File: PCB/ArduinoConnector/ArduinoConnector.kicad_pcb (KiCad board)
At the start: 2 copper layers, 0 parts

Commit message: New PCBs
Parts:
- added D1: 1N5819, Diode_SMD:D_SMA, F.Cu at (130.4, 84.0)
- added J1: Arduino, Connector_PinHeader_2.54mm:PinHeader_2x03_P2.54mm_Vertical, F.Cu at (120.2, 92.0)
- added J2: FAN, Connector_Molex:Molex_KK-254_AE-6410-04A_1x04_P2.54mm_Vertical, F.Cu at (128.7, 89.4)
- added Q1: MMBT100, Package_TO_SOT_SMD:SOT-23, F.Cu at (126.7, 85.6)
- added R1: 330, Resistor_SMD:R_0805_2012Metric, F.Cu at (126.7, 82.4)
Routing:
- net +5V: track 0.00 -> 18.7 mm
- net /POWER: track 0.00 -> 14.3 mm
- net /PWM: track 0.00 -> 9.60 mm
- net /SENSE: track 0.00 -> 9.55 mm
- net /FAN_GND: track 0.00 -> 7.80 mm
- net Net-(R1-Pad2): track 0.00 -> 2.28 mm
- net GND: vias 0 -> 6
- added copper zone on B.Cu, net GND
- added copper zone on F.Cu, net GND
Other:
- board outline added: 14.1 x 18.6 mm
- net class Default removed
- net class Power removed
- net class Signal removed

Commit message: Generated gerbers
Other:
- board text added: "ArduinoConnector v1"
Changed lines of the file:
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@@
   )
   (paper "A4")
+  (title_block
+    (title "ArduinoConnector")
+    (date "2022-03-13")
+    (rev "v1")
+  )
   (layers
     (0 "F.Cu" signal)
@@
     (pad_to_mask_clearance 0.0508)
     (pcbplotparams
-      (layerselection 0x0000030_80000001)
+      (layerselection 0x00010f0_ffffffff)
       (disableapertmacros false)
-      (usegerberextensions false)
+      (usegerberextensions true)
       (usegerberattributes true)
       (usegerberadvancedattributes true)
@@
       (outputformat 1)
       (mirror false)
-      (drillshape 1)
+      (drillshape 0)
       (scaleselection 1)
-      (outputdirectory "")
+      (outputdirectory "plots/")
     )
   )
@@
     (fp_line (start -1 0.625) (end -1 -0.625) (layer "F.Fab") (width 0.1))
     (fp_line (start 1 -0.625) (end 1 0.625) (layer "F.Fab") (width 0.1))
-    (pad "1" smd roundrect (at -0.9125 0) (size 1.025 1.4) (layers "F.Cu" "F.Paste" "F.Mask") (roundrect_rratio 0.243902)
+    (pad "1" smd roundrect (at -0.9125 0) (size 1.025 1.4) (layers "F.Cu" "F.Paste" "F.Mask") (roundrect_rratio 0.243902439)
       (net 3 "/POWER") (pintype "passive"))
-    (pad "2" smd roundrect (at 0.9125 0) (size 1.025 1.4) (layers "F.Cu" "F.Paste" "F.Mask") (roundrect_rratio 0.243902)
+    (pad "2" smd roundrect (at 0.9125 0) (size 1.025 1.4) (layers "F.Cu" "F.Paste" "F.Mask") (roundrect_rratio 0.243902439)
       (net 8 "Net-(R1-Pad2)") (pintype "passive"))
     (model "${KICAD6_3DMODEL_DIR}/Resistor_SMD.3dshapes/R_0805_2012Metric.wrl"
@@
     (fp_line (start -0.562893 0) (end -1.27 0.5) (layer "F.Fab") (width 0.1))
     (fp_line (start -1.27 -2.92) (end -1.27 2.88) (layer "F.Fab") (width 0.1))
-    (pad "1" thru_hole roundrect (at 0 0 270) (size 1.74 2.19) (drill 1.19) (layers *.Cu *.Mask) (roundrect_rratio 0.143678)
+    (pad "1" thru_hole roundrect (at 0 0 270) (size 1.74 2.19) (drill 1.19) (layers *.Cu *.Mask) (roundrect_rratio 0.1436781609)
       (net 2 "/FAN_GND") (pinfunction "Pin_1") (pintype "passive"))
     (pad "2" thru_hole oval (at 2.54 0 270) (size 1.74 2.19) (drill 1.19) (layers *.Cu *.Mask)
@@
   (gr_line (start 124.7 90) (end 124.7 80.4) (layer "Edge.Cuts") (width 0.15))
   (gr_line (start 124.7 80.4) (end 132.4 80.4) (layer "Edge.Cuts") (width 0.15))
-  (dimension (type aligned) (layer "F.Cu")
+  (gr_text "ArduinoConnector v1" (at 130.8 89.9 90) (layer "B.SilkS")
+    (effects (font (size 1 1) (thickness 0.15)) (justify mirror))
+  )
+  (dimension (type aligned) (layer "Dwgs.User")
     (pts (xy 132.4 99) (xy 132.4 80.4))
-    (height 5)
-    (gr_text "0.7323 in" (at 135.6 89.7 90) (layer "F.Cu")
+    (height 5.2)
+    (gr_text "18.6000 mm" (at 135.8 89.7 90) (layer "Dwgs.User")
       (effects (font (size 1.5 1.5) (thickness 0.3)))
     )
@@
     (style (thickness 0.2) (arrow_length 1.27) (text_position_mode 0) (extension_height 0.58642) (extension_offset 0.5) keep_text_aligned)
   )
-  (dimension (type aligned) (layer "F.Cu")
+  (dimension (type aligned) (layer "Dwgs.User")
     (pts (xy 118.3 99) (xy 132.4 99))
     (height 5.6)
-    (gr_text "0.5551 in" (at 125.35 102.8) (layer "F.Cu")
+    (gr_text "14.1000 mm" (at 125.35 102.8) (layer "Dwgs.User")
       (effects (font (size 1.5 1.5) (thickness 0.3)))
     )
@@
   (segment (start 127.6125 84.625) (end 127.65 84.6625) (width 0.2032) (layer "F.Cu") (net 8))
   (zone (net 7) (net_name "GND") (layers F&B.Cu) (name "GND") (hatch edge 0.508)
-    (connect_pads yes (clearance 0.2))
+    (connect_pads (clearance 0.2))
     (min_thickness 0.254) (filled_areas_thickness no)
     (fill yes (thermal_gap 0.508) (thermal_bridge_width 0.508))

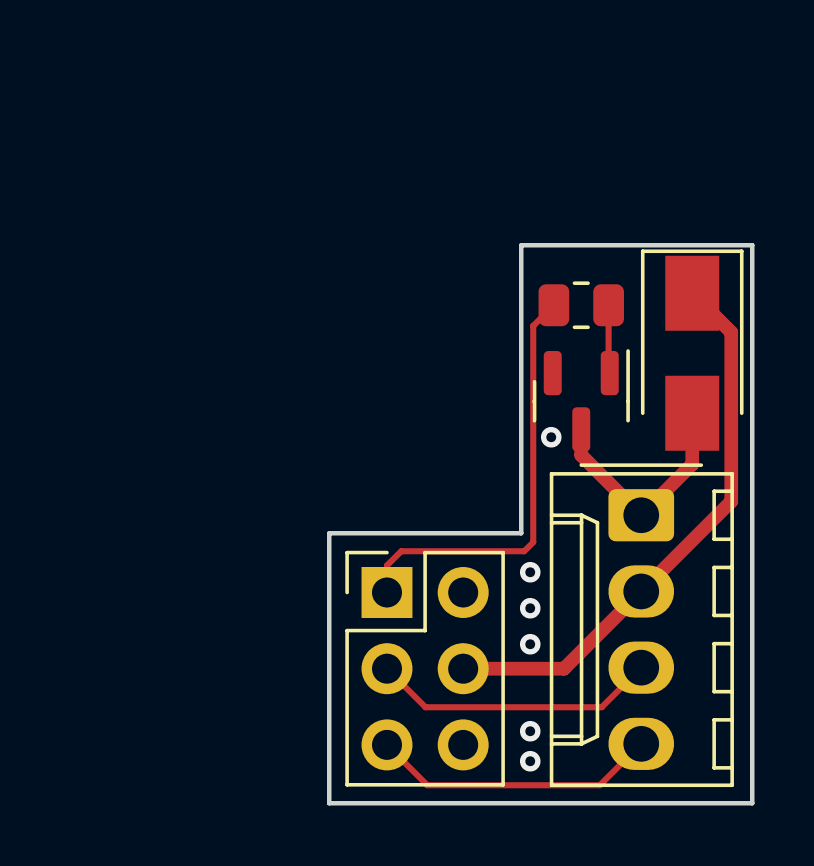
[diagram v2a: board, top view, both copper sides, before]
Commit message: Changed pin assignments and redid the PCB
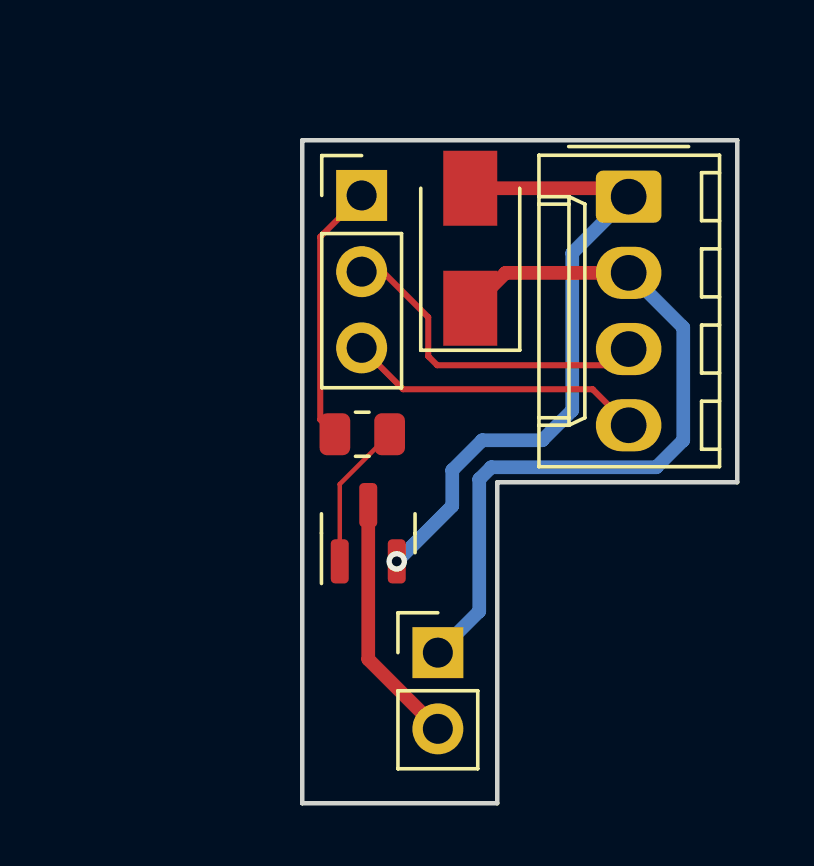
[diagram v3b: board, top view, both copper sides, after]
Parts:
- added J2: Ard2, Connector_PinHeader_2.54mm:PinHeader_1x02_P2.54mm_Vertical, F.Cu at (121.9, 94.0)
- J1: value Arduino -> Ard1; footprint Connector_PinHeader_2.54mm:PinHeader_2x03_P2.54mm_Vertical -> Connector_PinHeader_2.54mm:PinHeader_1x03_P2.54mm_Vertical
- moved J1 13.3 mm to (119.4, 78.7)
- moved J3 10.6 mm to (128.3, 78.8)
- moved R1 8.47 mm to (119.4, 86.7)
- moved Q1 8.35 mm to (119.6, 90.0), turned to 90 degrees
- moved D1 8.19 mm to (123.0, 80.5), turned to 90 degrees
- renumbered J2 to J3
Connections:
- J1 pad 2: unconnected-(J1-Pad2) -> /SENSE
- J1 pad 3: /SENSE -> /PWM
- Q1 pad 2: GND -> /FAN_GND
- Q1 pad 3: /FAN_GND -> GND
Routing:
- net /FAN_GND: track 7.80 -> 21.9 mm, vias 0 -> 1
- net GND: track 0.00 -> 8.42 mm, vias 6 -> 0
- net +5V: track 18.7 -> 25.8 mm
- net /POWER: track 14.3 -> 8.73 mm
- net Net-(Q1-Pad1): track 2.28 -> 4.93 mm
- net /SENSE: track 9.55 -> 11.2 mm
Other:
- board size 14.1 x 18.6 mm -> 14.5 x 22.1 mm
- board text added: "ArduinoConnector v2"
- board text removed: "ArduinoConnector v1"

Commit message: Fucking around with the PCB layout
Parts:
- moved R1 3.32 mm to (118.5, 89.9), turned to -90 degrees
- moved J1 2.54 mm to (119.4, 76.2)
- moved Q1 1.60 mm to (121.2, 89.9), turned to -90 degrees
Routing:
- net GND: track 8.42 -> 0.00 mm
- net /POWER: track 8.73 -> 13.6 mm
- net /PWM: track 9.97 -> 13.5 mm
- net /SENSE: track 11.2 -> 13.3 mm
- net /FAN_GND: track 21.9 -> 20.7 mm
- net Net-(Q1-Pad1): track 4.93 -> 4.42 mm
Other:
- board size 14.5 x 22.1 mm -> 14.5 x 24.7 mm
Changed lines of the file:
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@@
   (net 7 "GND")
   (footprint "Connector_PinHeader_2.54mm:PinHeader_1x03_P2.54mm_Vertical" (layer "F.Cu")
-    (at 119.38 78.74)
+    (at 119.38 76.2)
     (descr "Through hole straight pin header, 1x03, 2.54mm pitch, single row")
     (tags "Through hole pin header THT 1x03 2.54mm single row")
@@
   )
   (footprint "Package_TO_SOT_SMD:SOT-23" (layer "F.Cu")
-    (at 119.6 90 90)
+    (at 121.2 89.9 -90)
     (descr "SOT, 3 Pin (https://www.jedec.org/system/files/docs/to-236h.pdf variant AB), generated with kicad-footprint-generator ipc_gullwing_generator.py")
     (tags "SOT TO_SOT_SMD")
@@
     (fp_line (start 0.65 -1.45) (end 0.65 1.45) (layer "F.Fab") (width 0.1))
     (fp_line (start 0.65 1.45) (end -0.65 1.45) (layer "F.Fab") (width 0.1))
-    (pad "1" smd roundrect (at -0.9375 -0.95 90) (size 1.475 0.6) (layers "F.Cu" "F.Paste" "F.Mask") (roundrect_rratio 0.25)
+    (pad "1" smd roundrect (at -0.9375 -0.95 270) (size 1.475 0.6) (layers "F.Cu" "F.Paste" "F.Mask") (roundrect_rratio 0.25)
       (net 4 "Net-(Q1-Pad1)") (pinfunction "B") (pintype "input"))
-    (pad "2" smd roundrect (at -0.9375 0.95 90) (size 1.475 0.6) (layers "F.Cu" "F.Paste" "F.Mask") (roundrect_rratio 0.25)
+    (pad "2" smd roundrect (at -0.9375 0.95 270) (size 1.475 0.6) (layers "F.Cu" "F.Paste" "F.Mask") (roundrect_rratio 0.25)
       (net 2 "/FAN_GND") (pinfunction "E") (pintype "passive"))
-    (pad "3" smd roundrect (at 0.9375 0 90) (size 1.475 0.6) (layers "F.Cu" "F.Paste" "F.Mask") (roundrect_rratio 0.25)
+    (pad "3" smd roundrect (at 0.9375 0 270) (size 1.475 0.6) (layers "F.Cu" "F.Paste" "F.Mask") (roundrect_rratio 0.25)
       (net 7 "GND") (pinfunction "C") (pintype "passive"))
     (model "${KICAD6_3DMODEL_DIR}/Package_TO_SOT_SMD.3dshapes/SOT-23.wrl"
@@
   )
   (footprint "Resistor_SMD:R_0805_2012Metric" (layer "F.Cu")
-    (at 119.4 86.7)
+    (at 118.5 89.9 -90)
     (descr "Resistor SMD 0805 (2012 Metric), square (rectangular) end terminal, IPC_7351 nominal, (Body size source: IPC-SM-782 page 72, https://www.pcb-3d.com/wordpress/wp-content/uploads/ipc-sm-782a_amendment_1_and_2.pdf), generated with kicad-footprint-generator")
     (tags "resistor")
@@
     (property "Sheetname" "")
     (attr smd)
-    (fp_text reference "R1" (at 0 -1.65) (layer "F.SilkS") hide
-      (effects (font (size 1 1) (thickness 0.15)))
-    )
-    (fp_text value "330" (at 0 1.65) (layer "F.Fab") hide
-      (effects (font (size 1 1) (thickness 0.15)))
-    )
-    (fp_text user "${REFERENCE}" (at 0 0) (layer "F.Fab")
+    (fp_text reference "R1" (at 0 -1.65 90) (layer "F.SilkS") hide
+      (effects (font (size 1 1) (thickness 0.15)))
+    )
+    (fp_text value "330" (at 0 1.65 90) (layer "F.Fab") hide
+      (effects (font (size 1 1) (thickness 0.15)))
+    )
+    (fp_text user "${REFERENCE}" (at 0 0 90) (layer "F.Fab")
       (effects (font (size 0.5 0.5) (thickness 0.08)))
     )
@@
     (fp_line (start -1 0.625) (end -1 -0.625) (layer "F.Fab") (width 0.1))
     (fp_line (start 1 -0.625) (end 1 0.625) (layer "F.Fab") (width 0.1))
-    (pad "1" smd roundrect (at -0.9125 0) (size 1.025 1.4) (layers "F.Cu" "F.Paste" "F.Mask") (roundrect_rratio 0.243902439)
+    (pad "1" smd roundrect (at -0.9125 0 270) (size 1.025 1.4) (layers "F.Cu" "F.Paste" "F.Mask") (roundrect_rratio 0.243902439)
       (net 3 "/POWER") (pintype "passive"))
-    (pad "2" smd roundrect (at 0.9125 0) (size 1.025 1.4) (layers "F.Cu" "F.Paste" "F.Mask") (roundrect_rratio 0.243902439)
+    (pad "2" smd roundrect (at 0.9125 0 270) (size 1.025 1.4) (layers "F.Cu" "F.Paste" "F.Mask") (roundrect_rratio 0.243902439)
       (net 4 "Net-(Q1-Pad1)") (pintype "passive"))
     (model "${KICAD6_3DMODEL_DIR}/Resistor_SMD.3dshapes/R_0805_2012Metric.wrl"
@@
     )
   )
-  (gr_line (start 117.4 76.9) (end 131.9 76.9) (layer "Edge.Cuts") (width 0.15))
+  (gr_line (start 117.4 74.3) (end 121.4 74.3) (layer "Edge.Cuts") (width 0.15))
   (gr_line (start 131.9 76.9) (end 131.9 88.3) (layer "Edge.Cuts") (width 0.15))
   (gr_line (start 123.9 99) (end 117.4 99) (layer "Edge.Cuts") (width 0.15))
-  (gr_line (start 117.4 99) (end 117.4 76.9) (layer "Edge.Cuts") (width 0.15))
+  (gr_line (start 121.4 76.9) (end 131.9 76.9) (layer "Edge.Cuts") (width 0.15))
+  (gr_line (start 117.4 99) (end 117.4 74.3) (layer "Edge.Cuts") (width 0.15))
   (gr_line (start 123.9 99) (end 123.9 88.3) (layer "Edge.Cuts") (width 0.15))
+  (gr_line (start 121.4 74.3) (end 121.4 76.9) (layer "Edge.Cuts") (width 0.15))
   (gr_line (start 123.9 88.3) (end 131.9 88.3) (layer "Edge.Cuts") (width 0.15))
   (gr_text "ArduinoConnector v2" (at 122.2 85 90) (layer "B.SilkS")
@@
   )
   (dimension (type aligned) (layer "Dwgs.User")
-    (pts (xy 117.4 76.9) (xy 117.4 99))
+    (pts (xy 117.4 74.3) (xy 117.4 99))
     (height 3.599058)
-    (gr_text "0.8701 in" (at 112.650942 87.95 90) (layer "Dwgs.User")
+    (gr_text "0.9724 in" (at 112.650942 86.65 90) (layer "Dwgs.User")
       (effects (font (size 1 1) (thickness 0.15)))
     )
@@
   )
   (dimension (type aligned) (layer "Dwgs.User")
-    (pts (xy 117.4 76.9) (xy 131.9 76.9))
-    (height -3.1)
-    (gr_text "0.5709 in" (at 124.65 72.65) (layer "Dwgs.User")
+    (pts (xy 117.4 74.3) (xy 131.9 74.3))
+    (height -3.9)
+    (gr_text "0.5709 in" (at 124.65 69.25) (layer "Dwgs.User")
       (effects (font (size 1 1) (thickness 0.15)))
     )
@@
   (segment (start 123 78.5) (end 128 78.5) (width 0.4572) (layer "F.Cu") (net 2))
   (segment (start 128 78.5) (end 128.28 78.78) (width 0.4572) (layer "F.Cu") (net 2))
-  (via (at 120.55 90.9375) (size 0.6858) (drill 0.3302) (layers "F.Cu" "B.Cu") (net 2))
+  (via (at 120.25 88.9625) (size 0.6858) (drill 0.3302) (layers "F.Cu" "B.Cu") (net 2))
+  (segment (start 126.4 80.66) (end 126.4 85.9) (width 0.4572) (layer "B.Cu") (net 2))
+  (segment (start 125.4 86.9) (end 122.3125 86.9) (width 0.4572) (layer "B.Cu") (net 2))
+  (segment (start 122.3125 86.9) (end 120.25 88.9625) (width 0.4572) (layer "B.Cu") (net 2))
   (segment (start 128.28 78.78) (end 126.4 80.66) (width 0.4572) (layer "B.Cu") (net 2))
-  (segment (start 123.4 86.9) (end 122.4 87.9) (width 0.4572) (layer "B.Cu") (net 2))
-  (segment (start 122.4 87.9) (end 122.4 89.0875) (width 0.4572) (layer "B.Cu") (net 2))
-  (segment (start 125.4 86.9) (end 123.4 86.9) (width 0.4572) (layer "B.Cu") (net 2))
-  (segment (start 126.4 80.66) (end 126.4 85.9) (width 0.4572) (layer "B.Cu") (net 2))
   (segment (start 126.4 85.9) (end 125.4 86.9) (width 0.4572) (layer "B.Cu") (net 2))
-  (segment (start 122.4 89.0875) (end 120.55 90.9375) (width 0.4572) (layer "B.Cu") (net 2))
-  (segment (start 118 86.2125) (end 118 80.12) (width 0.2032) (layer "F.Cu") (net 3))
-  (segment (start 118.4875 86.7) (end 118 86.2125) (width 0.2032) (layer "F.Cu") (net 3))
-  (segment (start 118 80.12) (end 119.38 78.74) (width 0.2032) (layer "F.Cu") (net 3))
-  (segment (start 118.65 88.3625) (end 120.3125 86.7) (width 0.1524) (layer "F.Cu") (net 4))
-  (segment (start 118.65 90.9375) (end 118.65 88.3625) (width 0.1524) (layer "F.Cu") (net 4))
-  (segment (start 121.6 84.1) (end 121.9 84.4) (width 0.2032) (layer "F.Cu") (net 5))
-  (segment (start 120.08 81.28) (end 121.6 82.8) (width 0.2032) (layer "F.Cu") (net 5))
-  (segment (start 121.6 82.8) (end 121.6 84.1) (width 0.2032) (layer "F.Cu") (net 5))
-  (segment (start 121.9 84.4) (end 127.74 84.4) (width 0.2032) (layer "F.Cu") (net 5))
-  (segment (start 127.74 84.4) (end 128.28 83.86) (width 0.2032) (layer "F.Cu") (net 5))
-  (segment (start 119.38 81.28) (end 120.08 81.28) (width 0.2032) (layer "F.Cu") (net 5))
-  (segment (start 127.08 85.2) (end 128.28 86.4) (width 0.2032) (layer "F.Cu") (net 6))
-  (segment (start 120.76 85.2) (end 127.08 85.2) (width 0.2032) (layer "F.Cu") (net 6))
-  (segment (start 119.38 83.82) (end 120.76 85.2) (width 0.2032) (layer "F.Cu") (net 6))
-  (segment (start 119.6 89.0625) (end 119.6 94.2) (width 0.4572) (layer "F.Cu") (net 7))
-  (segment (start 119.6 94.2) (end 121.92 96.52) (width 0.4572) (layer "F.Cu") (net 7))
+  (segment (start 118 88.4875) (end 118 77.58) (width 0.2032) (layer "F.Cu") (net 3))
+  (segment (start 118 77.58) (end 119.38 76.2) (width 0.2032) (layer "F.Cu") (net 3))
+  (segment (start 118.5 88.9875) (end 118 88.4875) (width 0.2032) (layer "F.Cu") (net 3))
+  (segment (start 119.8875 90.8125) (end 118.5 90.8125) (width 0.1524) (layer "F.Cu") (net 4))
+  (segment (start 121.7375 88.9625) (end 119.8875 90.8125) (width 0.1524) (layer "F.Cu") (net 4))
+  (segment (start 122.15 88.9625) (end 121.7375 88.9625) (width 0.1524) (layer "F.Cu") (net 4))
+  (segment (start 121.6 84.1) (end 121.6 80.96) (width 0.2032) (layer "F.Cu") (net 5))
+  (segment (start 128.28 83.86) (end 127.74 84.4) (width 0.2032) (layer "F.Cu") (net 5))
+  (segment (start 121.6 80.96) (end 119.38 78.74) (width 0.2032) (layer "F.Cu") (net 5))
+  (segment (start 127.74 84.4) (end 121.9 84.4) (width 0.2032) (layer "F.Cu") (net 5))
+  (segment (start 121.9 84.4) (end 121.6 84.1) (width 0.2032) (layer "F.Cu") (net 5))
+  (segment (start 120.3 86.4) (end 119.38 85.48) (width 0.2032) (layer "F.Cu") (net 6))
+  (segment (start 128.28 86.4) (end 120.3 86.4) (width 0.2032) (layer "F.Cu") (net 6))
+  (segment (start 119.38 85.48) (end 119.38 81.28) (width 0.2032) (layer "F.Cu") (net 6))
   (zone (net 7) (net_name "GND") (layers F&B.Cu) (name "GND") (hatch edge 0.508)
     (connect_pads (clearance 0.2))
@@
         (xy 123.9 99)
         (xy 117.4 99)
-        (xy 117.4 76.9)
-        (xy 131.9 76.9)
+        (xy 117.4 74.3)
+        (xy 131.9 74.3)
         (xy 131.9 88.3)
       )

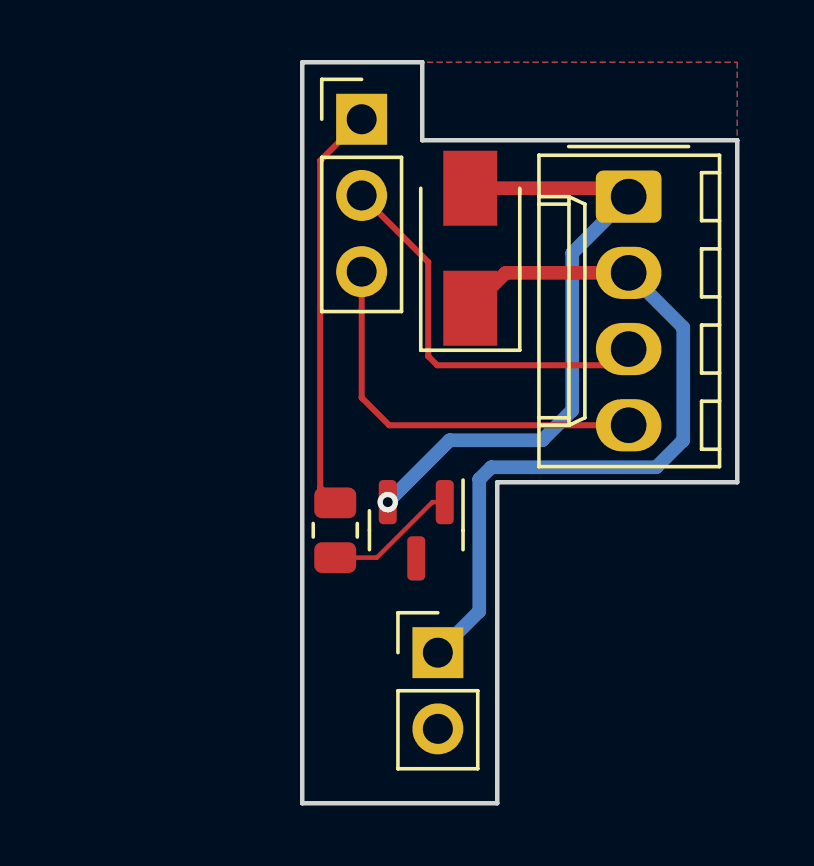
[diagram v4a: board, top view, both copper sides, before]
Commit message: New version of the ArduinoConnector
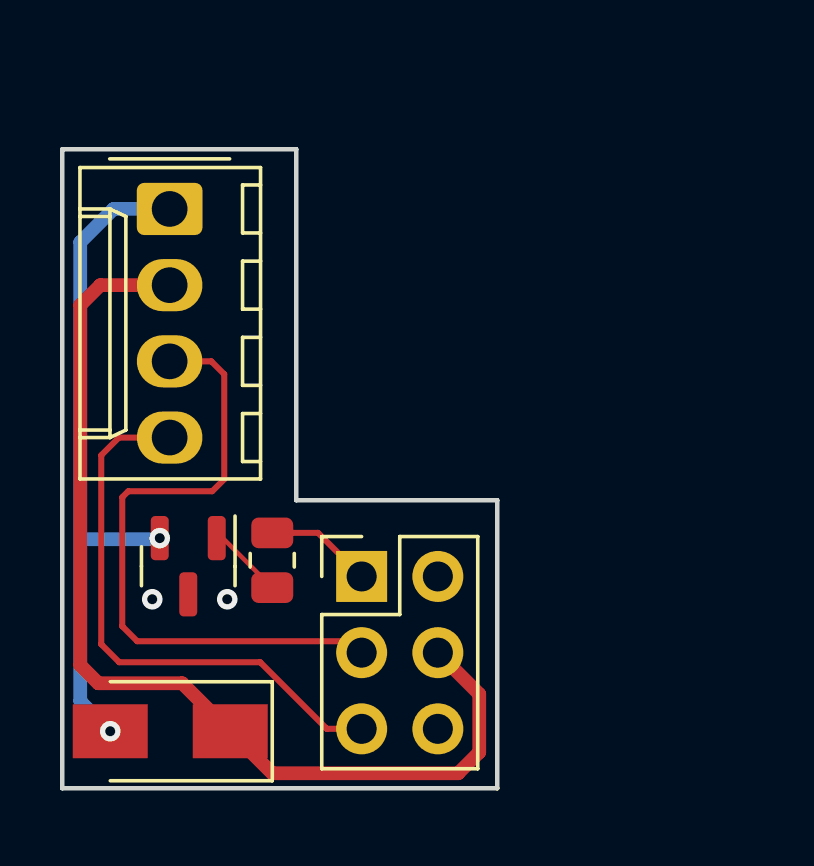
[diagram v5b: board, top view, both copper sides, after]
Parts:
- removed the J2 at (121.9, 94.0)
- J1: value Ard1 -> Arduino; footprint Connector_PinHeader_2.54mm:PinHeader_1x03_P2.54mm_Vertical -> Connector_PinHeader_2.54mm:PinHeader_2x03_P2.54mm_Vertical
- moved D1 19.0 mm to (113.0, 96.6), turned to 180 degrees
- moved J2 15.3 mm to (113.0, 79.2)
- moved J1 15.2 mm to (119.4, 91.4)
- moved Q1 7.69 mm to (113.6, 91.1)
- moved R1 2.33 mm to (116.4, 90.9)
- renumbered J3 to J2
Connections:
- J1 pad 2: /SENSE -> unconnected-(J1-Pad2)
- J1 pad 3: /PWM -> /SENSE
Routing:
- net /POWER: track 13.6 -> 3.58 mm
- net /SENSE: track 13.3 -> 21.8 mm
- net +5V: track 25.8 -> 34.2 mm
- net /PWM: track 13.5 -> 18.7 mm
- net /FAN_GND: track 20.7 -> 22.8 mm, vias 1 -> 2
- net Net-(Q1-Pad1): track 4.42 -> 2.53 mm
- net GND: vias 0 -> 2
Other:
- board size 14.5 x 24.7 mm -> 14.5 x 21.3 mm
